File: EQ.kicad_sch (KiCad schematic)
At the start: 36 parts, among them J1 USB_C_Receptacle_USB2.0_16P, J2 USB_B, J3 AudioJack3, SW1 PLAY/PAUSE, SW2 NEXT, SW3 PREVIOUS, U1 PCM2706PJT, Y1 12MHz

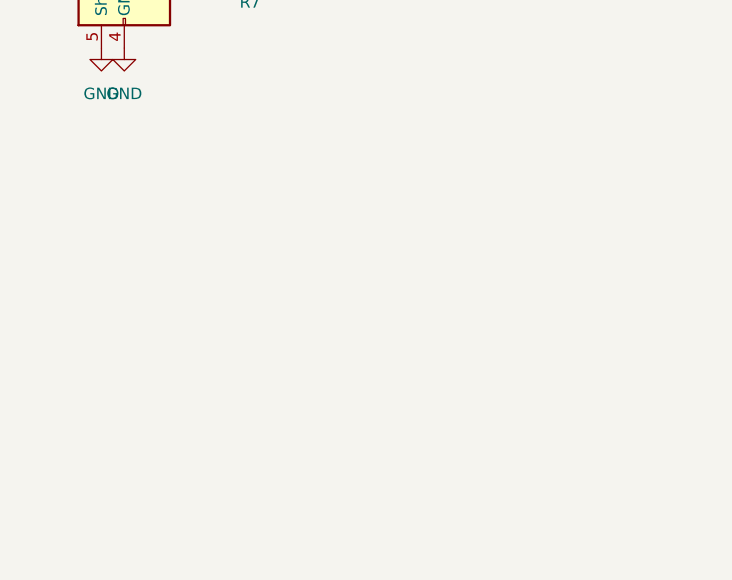
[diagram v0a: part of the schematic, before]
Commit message: OPampを回路図に配置
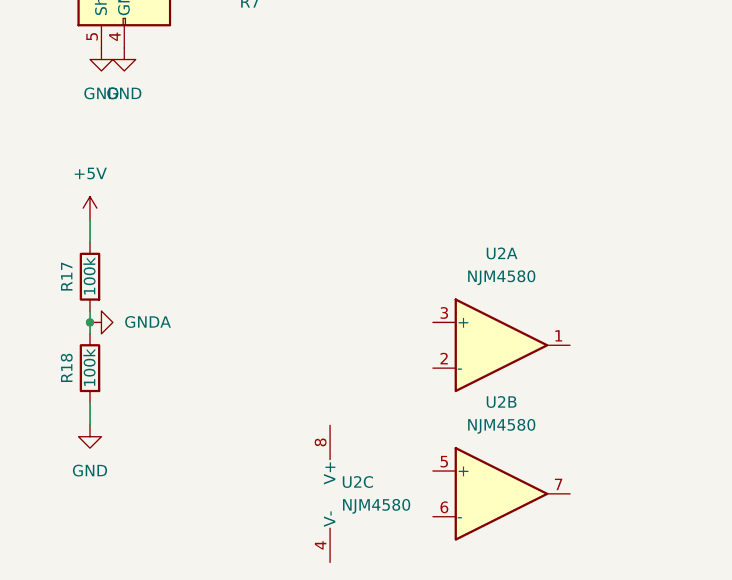
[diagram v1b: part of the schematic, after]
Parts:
- added R17, R18: 100k, Resistor_SMD:R_0603_1608Metric_Pad0.98x0.95mm_HandSolder, symbol Device:R
- added U2: NJM4580, Package_SO:SOIC-8_3.9x4.9mm_P1.27mm, symbol Amplifier_Operational:NJM4580
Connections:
- net +5V: now also R17.1
- net GND: now also R18.2
- new net GNDA: R17.2, R18.1
